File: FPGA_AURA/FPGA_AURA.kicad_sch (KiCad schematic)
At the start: 0 parts

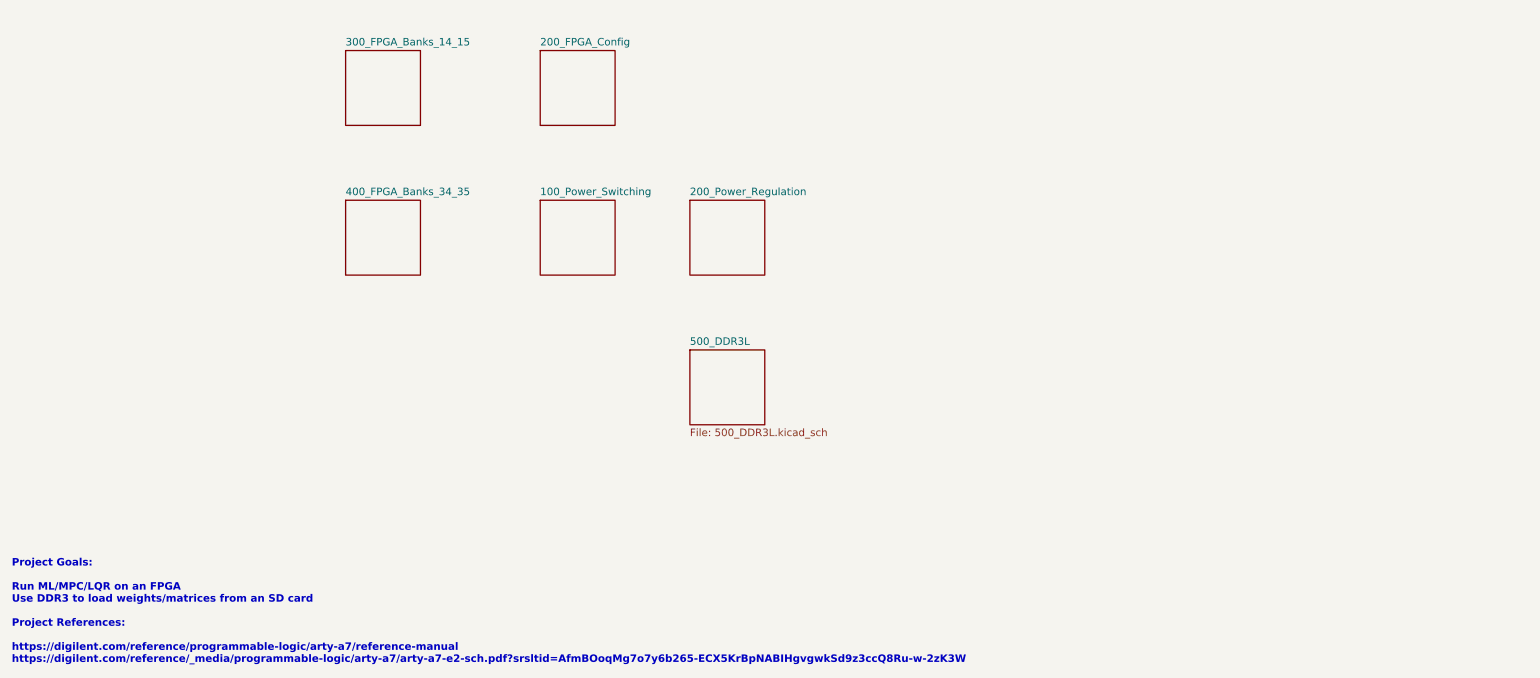
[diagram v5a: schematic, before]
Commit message: Added Connectors, FPGA Power and organized sheets.
All schematic sheets now go up in order with the correct prefix.
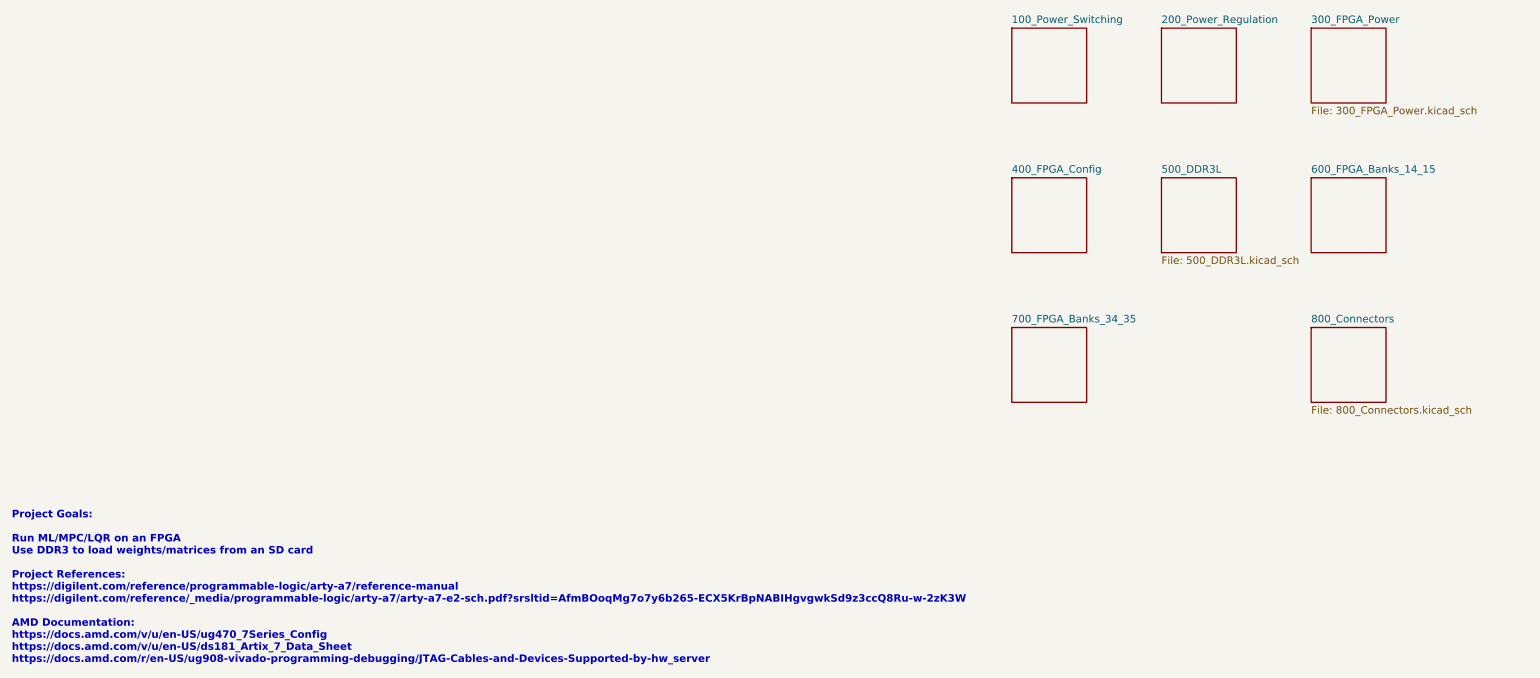
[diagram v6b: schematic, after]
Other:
- sheet 200_FPGA_Config renamed 400_FPGA_Config
- sheet 300_FPGA_Banks_14_15 renamed 600_FPGA_Banks_14_15
- sheet 400_FPGA_Banks_34_35 renamed 700_FPGA_Banks_34_35
- added sheet 300_FPGA_Power (300_FPGA_Power.kicad_sch)
- added sheet 800_Connectors (800_Connectors.kicad_sch)
- note added: "Project Goals: Run ML/MPC/LQR on an FPGA Use DDR3 to load weights/matrices from an SD card Project References: https://digilent.com/reference/programmable-logic/arty-a7/reference-manual https://digilent.com/reference/_media/programmable-logic/arty-a7/arty-a7-e2-sch.pdf?srsltid=AfmBOoqMg7o7y6b265-ECX5KrBpNABIHgvgwkSd9z3ccQ8Ru-w-2zK3W AMD Documentation: https://docs.amd.com/v/u/en-US/ug470_7Series_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"
- note removed: "Project Goals: Run ML/MPC/LQR on an FPGA Use DDR3 to load weights/matrices from an SD card Project References: https://digilent.com/reference/programmable-logic/arty-a7/reference-manual https://digilent.com/reference/_media/programmable-logic/arty-a7/arty-a7-e2-sch.pdf?srsltid=AfmBOoqMg7o7y6b265-ECX5KrBpNABIHgvgwkSd9z3ccQ8Ru-w-2zK3W"
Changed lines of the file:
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@@
 	(generator_version "9.0")
 	(paper "A4")
-	(text "Project Goals:\n\nRun ML/MPC/LQR on an FPGA\nUse DDR3 to load weights/matrices from an SD card\n\nProject References:\n\nhttps://digilent.com/reference/programmable-logic/arty-a7/reference-manual\nhttps://digilent.com/reference/_media/programmable-logic/arty-a7/arty-a7-e2-sch.pdf?srsltid=AfmBOoqMg7o7y6b265-ECX5KrBpNABIHgvgwkSd9z3ccQ8Ru-w-2zK3W\n"
+	(text "Project Goals:\n\nRun ML/MPC/LQR on an FPGA\nUse DDR3 to load weights/matrices from an SD card\n\nProject References:\nhttps://digilent.com/reference/programmable-logic/arty-a7/reference-manual\nhttps://digilent.com/reference/_media/programmable-logic/arty-a7/arty-a7-e2-sch.pdf?srsltid=AfmBOoqMg7o7y6b265-ECX5KrBpNABIHgvgwkSd9z3ccQ8Ru-w-2zK3W\n\nAMD Documentation:\nhttps://docs.amd.com/v/u/en-US/ug470_7Series_Config\nhttps://docs.amd.com/v/u/en-US/ds181_Artix_7_Data_Sheet\nhttps://docs.amd.com/r/en-US/ug908-vivado-programming-debugging/JTAG-Cables-and-Devices-Supported-by-hw_server\n"
 		(exclude_from_sim no)
 		(at 20.828 133.35 0)
@@
 	)
 	(sheet
-		(at 135.89 54.61)
+		(at 241.3 25.4)
 		(size 12.7 12.7)
 		(exclude_from_sim no)
@@
 			(color 0 0 0 0.0000)
 		)
-		(property "Sheetname" "200_Power_Regulation"
-			(at 135.89 53.8984 0)
+		(property "Sheetname" "300_FPGA_Power"
+			(at 241.3 24.6884 0)
 			(effects
 				(font
@@
 			)
 		)
-		(property "Sheetfile" "200_Power_Regulation.kicad_sch"
-			(at 135.89 67.8946 0)
+		(property "Sheetfile" "300_FPGA_Power.kicad_sch"
+			(at 241.3 38.6846 0)
 			(effects
 				(font
@@
 				)
 				(justify left top)
-				(hide yes)
 			)
 		)
@@
 			(project "FPGA_AURA"
 				(path "/3d83cb23-9528-4d06-8969-599520e9eb23"
-					(page "2")
+					(page "6")
 				)
 			)
@@
 	)
 	(sheet
-		(at 77.47 54.61)
+		(at 215.9 25.4)
 		(size 12.7 12.7)
 		(exclude_from_sim no)
@@
 			(color 0 0 0 0.0000)
 		)
-		(property "Sheetname" "400_FPGA_Banks_34_35"
-			(at 77.47 53.8984 0)
+		(property "Sheetname" "200_Power_Regulation"
+			(at 215.9 24.6884 0)
 			(effects
 				(font
@@
 			)
 		)
-		(property "Sheetfile" "400_FPGA_Banks_34_35.kicad_sch"
-			(at 77.47 67.8946 0)
+		(property "Sheetfile" "200_Power_Regulation.kicad_sch"
+			(at 215.9 38.6846 0)
 			(effects
 				(font
@@
 			(project "FPGA_AURA"
 				(path "/3d83cb23-9528-4d06-8969-599520e9eb23"
-					(page "4")
+					(page "3")
 				)
 			)
@@
 	)
 	(sheet
-		(at 135.89 80.01)
+		(at 190.5 76.2)
 		(size 12.7 12.7)
 		(exclude_from_sim no)
@@
 			(color 0 0 0 0.0000)
 		)
-		(property "Sheetname" "500_DDR3L"
-			(at 135.89 79.2984 0)
+		(property "Sheetname" "700_FPGA_Banks_34_35"
+			(at 190.5 75.4884 0)
 			(effects
 				(font
@@
 			)
 		)
-		(property "Sheetfile" "500_DDR3L.kicad_sch"
-			(at 135.89 93.2946 0)
+		(property "Sheetfile" "400_FPGA_Banks_34_35.kicad_sch"
+			(at 190.5 89.4846 0)
 			(effects
 				(font
@@
 				)
 				(justify left top)
+				(hide yes)
 			)
 		)
@@
 	)
 	(sheet
-		(at 77.47 29.21)
+		(at 215.9 50.8)
 		(size 12.7 12.7)
 		(exclude_from_sim no)
@@
 			(color 0 0 0 0.0000)
 		)
-		(property "Sheetname" "300_FPGA_Banks_14_15"
-			(at 77.47 28.4984 0)
+		(property "Sheetname" "500_DDR3L"
+			(at 215.9 50.0884 0)
 			(effects
 				(font
@@
 			)
 		)
-		(property "Sheetfile" "300_FPGA_Banks_14_15.kicad_sch"
-			(at 77.47 42.4946 0)
+		(property "Sheetfile" "500_DDR3L.kicad_sch"
+			(at 215.9 64.0846 0)
 			(effects
 				(font
@@
 				)
 				(justify left top)
-				(hide yes)
 			)
 		)
@@
 			(project "FPGA_AURA"
 				(path "/3d83cb23-9528-4d06-8969-599520e9eb23"
-					(page "3")
+					(page "5")
 				)
 			)
@@
 	)
 	(sheet
-		(at 110.49 29.21)
+		(at 241.3 50.8)
 		(size 12.7 12.7)
 		(exclude_from_sim no)
@@
 			(color 0 0 0 0.0000)
 		)
-		(property "Sheetname" "200_FPGA_Config"
-			(at 110.49 28.4984 0)
+		(property "Sheetname" "600_FPGA_Banks_14_15"
+			(at 241.3 50.0884 0)
 			(effects
 				(font
@@
 			)
 		)
-		(property "Sheetfile" "200_FPGA_Config.kicad_sch"
-			(at 110.49 42.4946 0)
+		(property "Sheetfile" "300_FPGA_Banks_14_15.kicad_sch"
+			(at 241.3 64.0846 0)
 			(effects
 				(font
@@
 			(project "FPGA_AURA"
 				(path "/3d83cb23-9528-4d06-8969-599520e9eb23"
-					(page "2")
+					(page "8")
 				)
 			)
@@
 	)
 	(sheet
-		(at 110.49 54.61)
+		(at 190.5 50.8)
 		(size 12.7 12.7)
 		(exclude_from_sim no)
@@
 			(color 0 0 0 0.0000)
 		)
-		(property "Sheetname" "100_Power_Switching"
-			(at 110.49 53.8984 0)
+		(property "Sheetname" "400_FPGA_Config"
+			(at 190.5 50.0884 0)
 			(effects
 				(font
@@
 			)
 		)
-		(property "Sheetfile" "100_Power_Switching.kicad_sch"
-			(at 110.49 67.8946 0)
+		(property "Sheetfile" "200_FPGA_Config.kicad_sch"
+			(at 190.5 64.0846 0)
 			(effects
 				(font
@@
 			(project "FPGA_AURA"
 				(path "/3d83cb23-9528-4d06-8969-599520e9eb23"
-					(page "1")
-				)
-			)
+					(page "4")
+				)
+			)
+		)
+	)
+	(sheet
+		(at 241.3 76.2)
+		(size 12.7 12.7)
+		(exclude_from_sim no)
+		(in_bom yes)
+		(on_board yes)
+		(dnp no)
+		(fields_autoplaced yes)
+		(stroke
+			(width 0.1524)
+			(type solid)
+		)
+		(fill
+			(color 0 0 0 0.0000)
+		)
+		(property "Sheetname" "800_Connectors"
+			(at 241.3 75.4884 0)
+			(effects
+				(font
+					(size 1.27 1.27)
+				)
+				(justify left bottom)
+			)
+		)
+		(property "Sheetfile" "800_Connectors.kicad_sch"
+			(at 241.3 89.4846 0)
+			(effects
+				(font
+					(size 1.27 1.27)
+				)
+				(justify left top)
+			)
+		)
+		(instances
+			(project "FPGA_AURA"
+				(path "/3d83cb23-9528-4d06-8969-599520e9eb23"
+					(page "9")
+				)
+			)
+		)
+	)
+	(sheet
+		(at 190.5 25.4)
+		(size 12.7 12.7)
+		(exclude_from_sim no)
+		(in_bom yes)
+		(on_board yes)
+		(dnp no)
+		(fields_autoplaced yes)
+		(stroke
+			(width 0.1524)
+			(type solid)
+		)
+		(fill
+			(color 0 0 0 0.0000)
+		)
+		(property "Sheetname" "100_Power_Switching"
+			(at 190.5 24.6884 0)
+			(effects
+				(font
+					(size 1.27 1.27)
+				)
+				(justify left bottom)
+			)
+		)
+		(property "Sheetfile" "100_Power_Switching.kicad_sch"
+			(at 190.5 38.6846 0)
+			(effects
+				(font
+					(size 1.27 1.27)
+				)
+				(justify left top)
+				(hide yes)
+			)
+		)
+		(instances
+			(project "FPGA_AURA"
+				(path "/3d83cb23-9528-4d06-8969-599520e9eb23"
+					(page "2")
+				)
+			)
